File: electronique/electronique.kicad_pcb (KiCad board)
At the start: 2 copper layers, 5 parts, among them J1 Conn_02x07_Odd_Even, U1 STM32L451RETx, U2 LD1117S50TR_SOT223, U3 LD1117S33TR_SOT223

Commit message: Schema change
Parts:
- added R1: R, Resistor_SMD:R_0805_2012Metric_Pad1.20x1.40mm_HandSolder, F.Cu at (132.1, 60.3)
- added R10: R, Resistor_SMD:R_0805_2012Metric_Pad1.20x1.40mm_HandSolder, F.Cu at (142.2, 40.6)
- added R11: R, Resistor_SMD:R_0805_2012Metric_Pad1.20x1.40mm_HandSolder, F.Cu at (142.6, 48.9)
- added R2: R, Resistor_SMD:R_0805_2012Metric_Pad1.20x1.40mm_HandSolder, F.Cu at (156.8, 38.1)
- added R3: R, Resistor_SMD:R_0805_2012Metric_Pad1.20x1.40mm_HandSolder, F.Cu at (156.6, 35.6)
- added R4: R, Resistor_SMD:R_0805_2012Metric_Pad1.20x1.40mm_HandSolder, F.Cu at (156.2, 32.4)
- added R5: R, Resistor_SMD:R_0805_2012Metric_Pad1.20x1.40mm_HandSolder, F.Cu at (156.8, 29.8)
- added R6: R, Resistor_SMD:R_0805_2012Metric_Pad1.20x1.40mm_HandSolder, F.Cu at (133.7, 48.3)
- added R7: R, Resistor_SMD:R_0805_2012Metric_Pad1.20x1.40mm_HandSolder, F.Cu at (142.9, 45.1)
- moved U3 36.4 mm to (135.9, 21.6), turned to 90 degrees
- moved D1 31.4 mm to (153.7, 24.1)
- moved U2 20.6 mm to (144.8, 26.7), turned to 180 degrees
- moved U1 12.7 mm to (132.1, 38.1), turned to 90 degrees
- moved J1 9.88 mm to (123.2, 54.1)
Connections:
- net Net-(BT1-Pad1) renamed +BATT
- net Net-(J1-Pad13) renamed /RX1
- net Net-(J1-Pad14) renamed /TX1
- net Net-(U1-Pad22) renamed /M1_PWM
- net Net-(U1-Pad34) renamed /M2N_PWM
- net Net-(U1-Pad35) renamed /M2_PWM
- net Net-(U1-Pad41) renamed /ECHO1
- net Net-(U1-Pad42) renamed /ECHO2
- net Net-(U1-Pad43) renamed /TRIG_US
- net Net-(U1-Pad44) renamed /ECHO3
- net Net-(U1-Pad46) renamed /SWDIO
- net Net-(U1-Pad49) renamed /SWCLK
- net Net-(U1-Pad50) renamed /CS
- net Net-(U1-Pad51) renamed /SCK
- net Net-(U1-Pad52) renamed /MISO
- net Net-(U1-Pad53) renamed /MOSI
- net Net-(U1-Pad54) renamed /XSHUT
- net Net-(U1-Pad58) renamed /M1N_PWM
- net Net-(U1-Pad61) renamed /SCL
- net Net-(U1-Pad62) renamed /SDA
- J1 pad 12: Net-(J1-Pad12) -> /NRST
- U1 pad 10: Net-(U1-Pad10) -> /PHOTOD3
- U1 pad 11: Net-(U1-Pad11) -> /PHOTOD4
- U1 pad 12: Net-(U1-Pad12) -> GND
- U1 pad 13: Net-(U1-Pad13) -> +3V3
- U1 pad 18: Net-(U1-Pad18) -> GND
- U1 pad 19: Net-(U1-Pad19) -> +3V3
- U1 pad 27: Net-(U1-Pad27) -> /PHOTOD
- U1 pad 28: Net-(U1-Pad28) -> /LED_A
- U1 pad 29: Net-(U1-Pad29) -> /LED_B
- U1 pad 30: Net-(U1-Pad30) -> /LED_C
- U1 pad 31: Net-(U1-Pad31) -> GND
- U1 pad 32: Net-(U1-Pad32) -> +3V3
- U1 pad 47: Net-(U1-Pad47) -> GND
- U1 pad 63: Net-(U1-Pad63) -> GND
- U1 pad 64: Net-(U1-Pad64) -> +3V3
- U1 pad 7: Net-(U1-Pad7) -> /NRST
- U1 pad 8: Net-(U1-Pad8) -> /PHOTOD1
- U1 pad 9: Net-(U1-Pad9) -> /PHOTOD2

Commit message: Schema mis a jour pour la seance de projet
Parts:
- added C1: C, Capacitor_SMD:C_0805_2012Metric_Pad1.15x1.40mm_HandSolder, F.Cu at (119.0, 53.0)
- added C2: C, Capacitor_SMD:C_0805_2012Metric_Pad1.15x1.40mm_HandSolder, F.Cu at (122.0, 53.0)
- added R8: R, Resistor_THT:R_Axial_DIN0207_L6.3mm_D2.5mm_P7.62mm_Horizontal, F.Cu at (107.4, 27.6)
- added R9: R, Resistor_THT:R_Axial_DIN0207_L6.3mm_D2.5mm_P7.62mm_Horizontal, F.Cu at (107.4, 31.6)
- moved R10 15.3 mm to (132.0, 52.0), turned to 90 degrees
- moved R7 9.75 mm to (136.0, 52.0), turned to 90 degrees
- moved J1 8.41 mm to (128.0, 61.0), turned to 90 degrees
- moved U3 6.06 mm to (130.0, 23.0)
- moved R6 6.02 mm to (129.0, 52.0), turned to 90 degrees
- moved R1 5.14 mm to (136.0, 57.0), turned to 90 degrees
- moved D1 4.12 mm to (150.0, 26.0)
- moved U2 4.08 mm to (143.0, 23.0), turned to 90 degrees
- moved R11 4.05 mm to (140.0, 52.0), turned to 90 degrees

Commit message: Schema/Routage presque finis
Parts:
- added BT1: 7.2V, Connector_PinHeader_2.54mm:PinHeader_2x01_P2.54mm_Vertical, F.Cu at (25.4, 14.0)
- added C11: .1uF, Capacitor_SMD:C_0805_2012Metric_Pad1.18x1.45mm_HandSolder, F.Cu at (71.0, 35.0)
- added C12: .1uF, Capacitor_SMD:C_0805_2012Metric_Pad1.18x1.45mm_HandSolder, F.Cu at (75.0, 67.0)
- added C13: 10uF, Capacitor_Tantalum_SMD:CP_EIA-2012-12_Kemet-R_Pad1.30x1.05mm_HandSolder, F.Cu at (56.0, 65.0)
- added C14: 1uF, Capacitor_Tantalum_SMD:CP_EIA-2012-12_Kemet-R_Pad1.30x1.05mm_HandSolder, F.Cu at (152.4, 86.7)
- added C15: .01uF, Capacitor_SMD:C_0805_2012Metric_Pad1.18x1.45mm_HandSolder, F.Cu at (154.9, 86.6)
- added C3: .1uF, Capacitor_SMD:C_0805_2012Metric_Pad1.18x1.45mm_HandSolder, F.Cu at (46.0, 65.0)
- added C4: 10uF, Capacitor_Tantalum_SMD:CP_EIA-2012-12_Kemet-R_Pad1.30x1.05mm_HandSolder, F.Cu at (45.0, 53.0)
- added C5: .1uF, Capacitor_SMD:C_0805_2012Metric_Pad1.18x1.45mm_HandSolder, F.Cu at (108.2, 52.1)
- added C6: 10uF, Capacitor_Tantalum_SMD:CP_EIA-2012-12_Kemet-R_Pad1.30x1.05mm_HandSolder, F.Cu at (45.0, 49.0)
- added C7: .1uF, Capacitor_SMD:C_0805_2012Metric_Pad1.18x1.45mm_HandSolder, F.Cu at (46.0, 61.0)
- added C8: 10uF, Capacitor_Tantalum_SMD:CP_EIA-2012-12_Kemet-R_Pad1.30x1.05mm_HandSolder, F.Cu at (45.0, 45.0)
- added FB1: Ferrite_Bead_Small, Ferrite_THT:LairdTech_28C0236-0JW-10, F.Cu at (147.3, 87.6)
- added J10: PHOTOD3, Connector_JST:JST_PH_B2B-PH-K_1x02_P2.00mm_Vertical, F.Cu at (45.7, 90.2)
- added J11: PHOTOD4, Connector_JST:JST_PH_B2B-PH-K_1x02_P2.00mm_Vertical, F.Cu at (58.4, 90.2)
- added J12: Ultrason 3, Connector_PinHeader_2.54mm:PinHeader_1x04_P2.54mm_Vertical, F.Cu at (142.2, 39.4)
- added J13: Moteur 2, Connector_JST:JST_PH_B6B-PH-K_1x06_P2.00mm_Vertical, F.Cu at (97.8, 33.0)
- added J14: Moteur 1, Connector_JST:JST_PH_B6B-PH-K_1x06_P2.00mm_Vertical, F.Cu at (62.2, 26.7)
- added J3: Camera, Connector_PinHeader_2.54mm:PinHeader_1x06_P2.54mm_Vertical, F.Cu at (130.8, 33.0)
- added J4: TOF1, Connector_PinHeader_2.54mm:PinHeader_2x05_P2.54mm_Vertical, F.Cu at (116.8, 22.9)
- added J5: Conn_01x06, Connector_PinHeader_2.54mm:PinHeader_1x06_P2.54mm_Vertical, F.Cu at (81.3, 86.4)
- added J6: Ultrason 1, Connector_PinHeader_2.54mm:PinHeader_1x04_P2.54mm_Vertical, F.Cu at (137.2, 39.4)
- added J7: PHOTOD1, Connector_JST:JST_PH_B2B-PH-K_1x02_P2.00mm_Vertical, F.Cu at (64.8, 90.2)
- added J8: PHOTOD2, Connector_JST:JST_PH_B2B-PH-K_1x02_P2.00mm_Vertical, F.Cu at (52.1, 90.2)
- added J9: Ultrason 2, Connector_PinHeader_2.54mm:PinHeader_1x04_P2.54mm_Vertical, F.Cu at (132.1, 39.4)
- added SW1: SW_Push, Button_Switch_THT:SW_PUSH_6mm, F.Cu at (90.2, 61.0)
- added U4: LB1930MC-AH, lumos_minima:LB1930MC-AH, F.Cu at (88.9, 25.4)
- added U5: LB1930MC-AH, lumos_minima:LB1930MC-AH, F.Cu at (53.3, 25.4)
- C1: value C -> .1uF; footprint Capacitor_SMD:C_0805_2012Metric_Pad1.15x1.40mm_HandSolder -> Capacitor_SMD:C_0805_2012Metric_Pad1.18x1.45mm_HandSolder
- C2: value C -> 10uF; footprint Capacitor_SMD:C_0805_2012Metric_Pad1.15x1.40mm_HandSolder -> Capacitor_Tantalum_SMD:CP_EIA-2012-12_Kemet-R_Pad1.30x1.05mm_HandSolder
- J1: value Conn_02x07_Odd_Even -> Conn_01x02; footprint FTSH:SAMTEC_FTSH-107-01-L-DV-K-A -> Connector_JST:JST_PH_B2B-PH-K_1x02_P2.00mm_Vertical
- U1: value STM32L451RETx -> LD1117S50TR_SOT223; footprint Package_QFP:LQFP-64_10x10mm_P0.5mm -> Package_TO_SOT_SMD:SOT-223-3_TabPin2
- U2: value LD1117S50TR_SOT223 -> LD1117S33TR_SOT223
- U3: value LD1117S33TR_SOT223 -> STM32L451RETx; footprint Package_TO_SOT_SMD:SOT-223-3_TabPin2 -> Package_QFP:LQFP-64_10x10mm_P0.5mm
- moved R4 119.5 mm to (41.0, 64.0)
- moved R3 118.4 mm to (40.0, 56.0)
- moved R2 117.9 mm to (41.0, 60.0), turned to 0 degrees
- moved U2 117.8 mm to (25.4, 30.5), turned to 0 degrees
- moved J1 111.8 mm to (22.9, 22.9), turned to 0 degrees
- moved D1 110.7 mm to (39.4, 22.9), turned to 180 degrees
- moved R10 98.0 mm to (44.7, 96.5), turned to 0 degrees
- moved R7 95.9 mm to (51.1, 96.5), turned to 0 degrees
- moved U1 95.6 mm to (36.8, 30.5), turned to 180 degrees
- moved R11 93.8 mm to (57.4, 96.5), turned to 0 degrees
- moved R6 79.0 mm to (63.8, 96.5), turned to 0 degrees
- moved C2 76.1 mm to (46.0, 57.0), turned to 0 degrees
- moved R1 74.7 mm to (66.0, 31.0), turned to 0 degrees
- moved U3 70.9 mm to (166.4, 83.8), turned to 0 degrees
- moved C1 69.1 mm to (51.0, 65.0), turned to 0 degrees
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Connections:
- C1 pad 1: GND -> +3V3
- C1 pad 2: Net-(C1-Pad2) -> GND
- C2 pad 1: Net-(C2-Pad1) -> +3V3
- R1 pad 1: Net-(J1-Pad11) -> Net-(J2-Pad11)
- U1 pad 1: Net-(U1-Pad1) -> GND
- U1 pad 2: Net-(U1-Pad2) -> +5V
- U1 pad 3: Net-(U1-Pad3) -> Net-(D1-Pad1)
- U2 pad 2: +5V -> +3V3
- U2 pad 3: Net-(D1-Pad1) -> +5V
- U3 pad 1: GND -> +3V3
- U3 pad 2: +3V3 -> Net-(U3-Pad2)
- U3 pad 3: +5V -> Net-(U3-Pad3)
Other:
- board outline added: 100 x 50 mm

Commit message: Schema/Routage presque finis
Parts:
- moved R10 110.6 mm to (153.7, 77.2), turned to 90 degrees
- moved R7 105.8 mm to (153.7, 70.8), turned to 90 degrees
- moved J10 102.6 mm to (147.3, 76.2), turned to 0 degrees
- moved R11 101.4 mm to (153.7, 64.5), turned to 90 degrees
- moved R6 97.7 mm to (153.7, 58.1), turned to 90 degrees
- moved J8 97.4 mm to (147.3, 69.8), turned to 0 degrees
- moved J11 92.8 mm to (147.3, 63.5), turned to 0 degrees
- moved J7 88.9 mm to (147.3, 57.1), turned to 0 degrees
- moved J12 85.5 mm to (223.5, 66.0)
- moved J6 85.5 mm to (218.4, 66.0)
- moved J9 85.5 mm to (213.4, 66.0)
- moved SW1 70.1 mm to (160.0, 67.3)
- moved J3 66.0 mm to (195.6, 45.7)
- moved U3 32.9 mm to (195.6, 68.6)

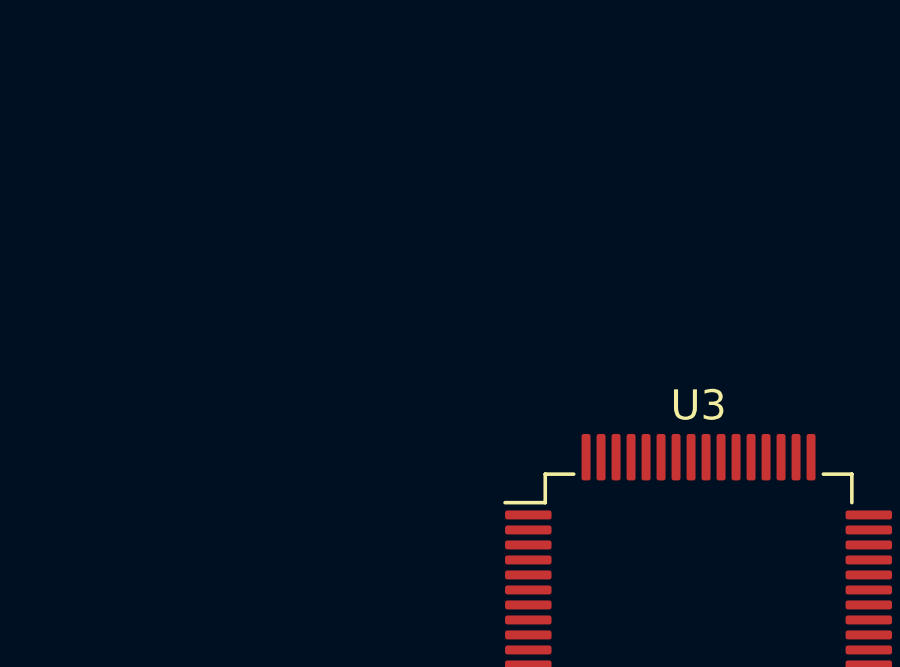
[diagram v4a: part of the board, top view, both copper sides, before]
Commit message: Ajout de l'ampli de captage de courant MAX40056.
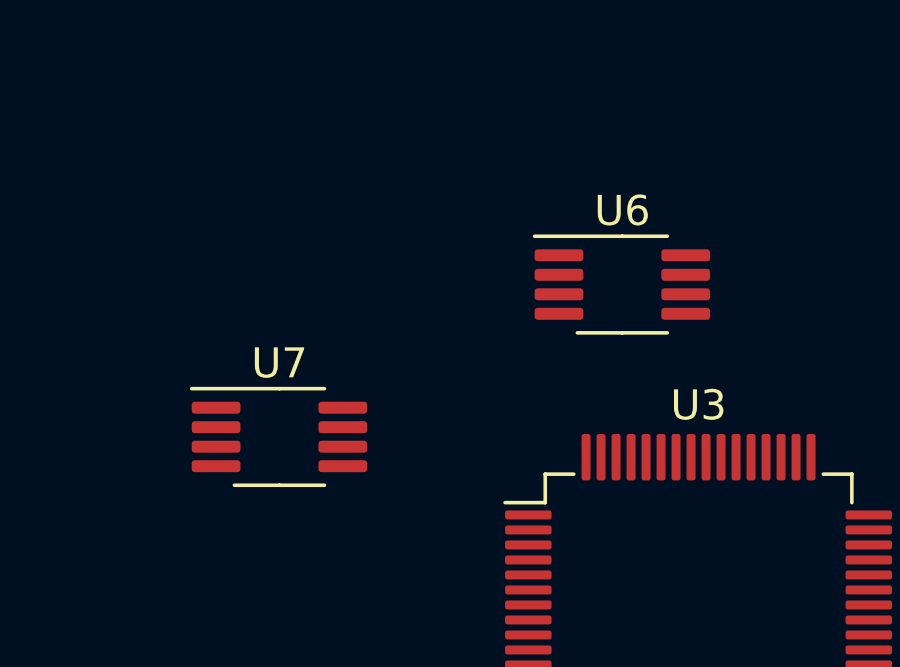
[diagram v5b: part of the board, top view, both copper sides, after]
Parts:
- added U6: MAX40056FAUA+, Package_SO:MSOP-8_3x3mm_P0.65mm, F.Cu at (193.0, 57.1)
- added U7: MAX40056FAUA+, Package_SO:MSOP-8_3x3mm_P0.65mm, F.Cu at (181.6, 62.2)
- R8, R9: value R -> 30m

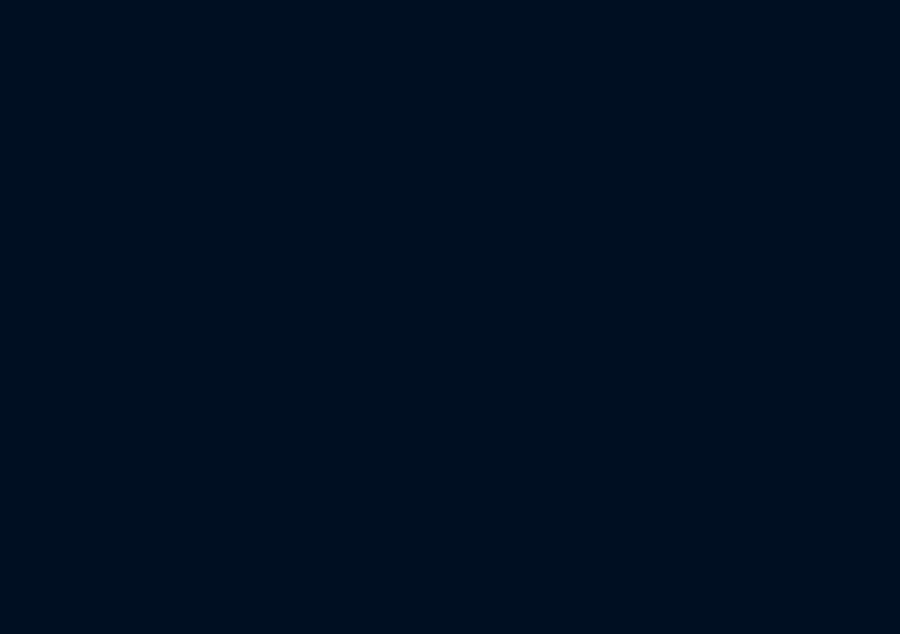
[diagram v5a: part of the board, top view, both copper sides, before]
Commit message: Cablage preliminaire des capteurs de courant
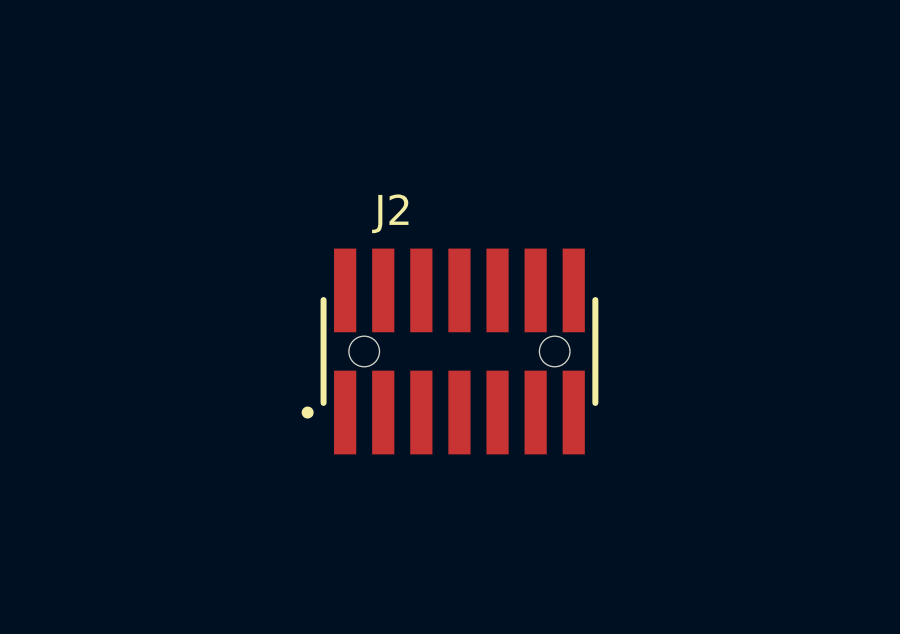
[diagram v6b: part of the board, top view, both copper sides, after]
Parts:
- added J2: Conn_02x07_Odd_Even, lumos_minima:SAMTEC_FTSH-107-01-L-DV-K-A, F.Cu at (137.2, 26.7)
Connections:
- net Net-(U6-Pad4) renamed /I_SENS1
- net Net-(U7-Pad4) renamed /I_SENS2
- J13 pad 1: Net-(J13-Pad1) -> /RSN2
- J14 pad 1: Net-(J14-Pad1) -> /RSN1
- R8 pad 1: Net-(J13-Pad1) -> /RSN2
- R8 pad 2: Net-(R8-Pad2) -> /RSP2
- R9 pad 1: Net-(J14-Pad1) -> /RSN1
- R9 pad 2: Net-(R9-Pad2) -> /RSP1
- U4 pad 9: Net-(R8-Pad2) -> /RSP2
- U5 pad 9: Net-(R9-Pad2) -> /RSP1
- U6 pad 1: Net-(U6-Pad1) -> /RSP1
- U6 pad 3: Net-(U6-Pad3) -> +3V3
- U6 pad 6: Net-(U6-Pad6) -> GND
- U6 pad 8: Net-(U6-Pad8) -> /RSN1
- U7 pad 1: Net-(U7-Pad1) -> /RSP2
- U7 pad 3: Net-(U7-Pad3) -> +3V3
- U7 pad 6: Net-(U7-Pad6) -> GND
- U7 pad 8: Net-(U7-Pad8) -> /RSN2

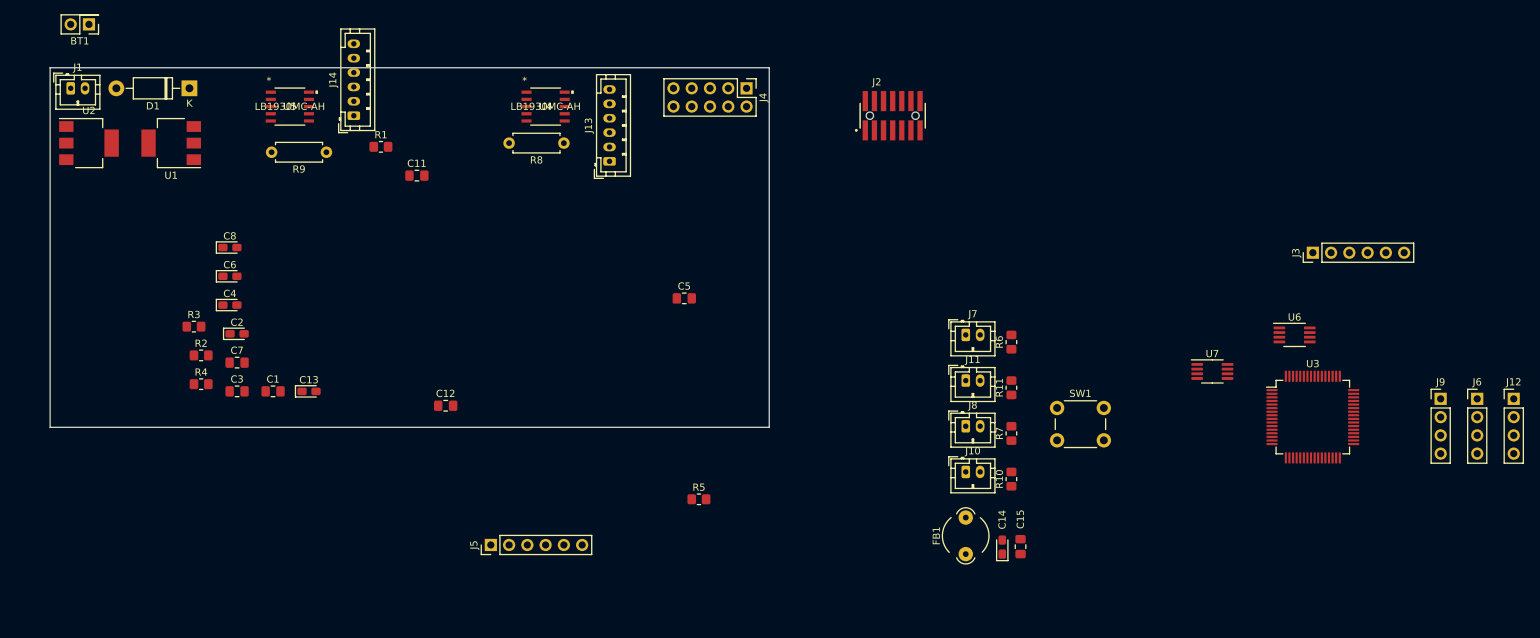
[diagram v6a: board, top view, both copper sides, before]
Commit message: Schema de concept termine, il manque les valeurs de certains condensateurs, il est possible qu'il y aie besoin de plus de condensateurs.
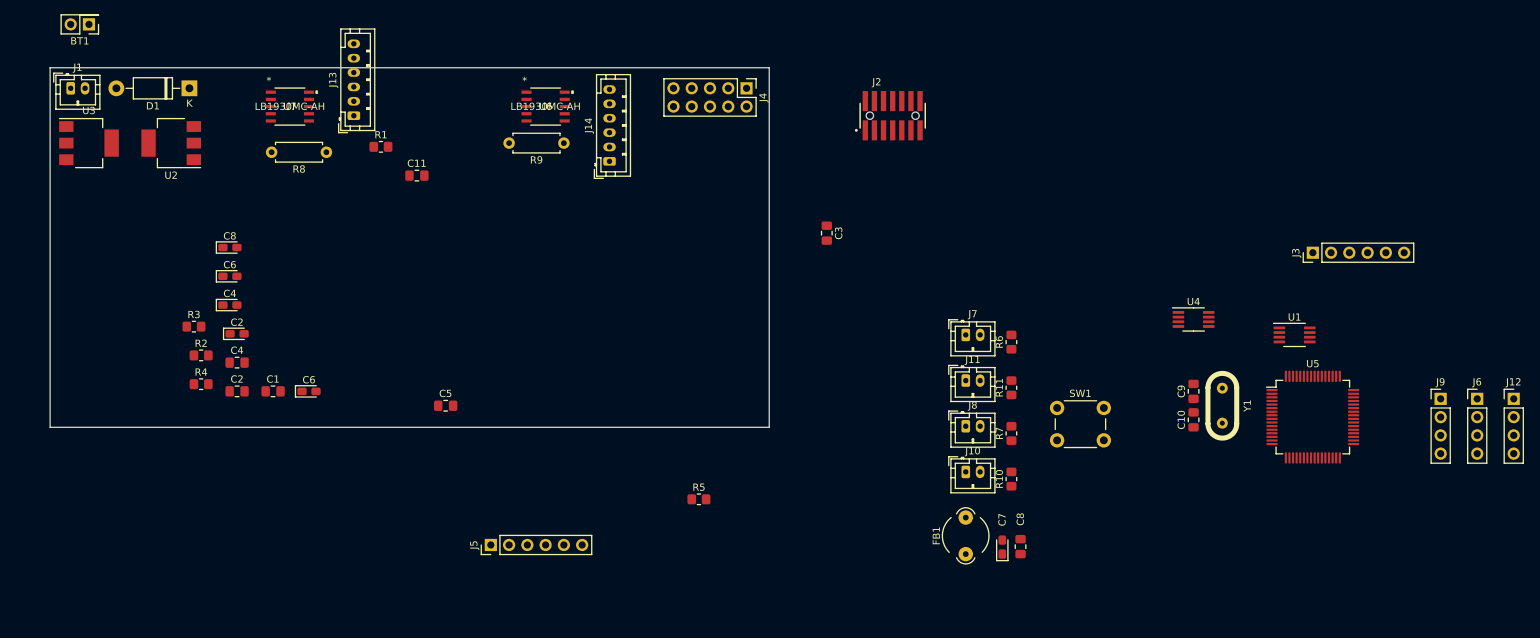
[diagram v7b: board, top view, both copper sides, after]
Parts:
- added C10: C, Capacitor_SMD:C_0805_2012Metric_Pad1.18x1.45mm_HandSolder, F.Cu at (179.0, 69.0)
- added C9: C, Capacitor_SMD:C_0805_2012Metric_Pad1.18x1.45mm_HandSolder, F.Cu at (179.0, 65.0)
- added Y1: LFXTAL003240, lumos_minima:HC494H, F.Cu at (183.0, 67.0)
- moved C3 21.8 mm to (128.0, 43.0), turned to 270 degrees
- moved U4 7.69 mm to (179.0, 55.0)
- renumbered C3 to C2, C5 to C3, C7 to C4, C12 to C5, C13 to C6, C14 to C7, C15 to C8, J14 to J13, J13 to J14, R9 to R8, R8 to R9, U6 to U1, U1 to U2, U2 to U3, U7 to U4, U3 to U5, U4 to U6, U5 to U7
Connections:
- R2 pad 2: /PHOTOD -> /PHOTOD_COUL
- U5 pad 14: Net-(U3-Pad14) -> /M2_A
- U5 pad 15: Net-(U3-Pad15) -> /M2_B
- U5 pad 23: Net-(U3-Pad23) -> /I_SENS1
- U5 pad 24: Net-(U3-Pad24) -> /I_SENS2
- U5 pad 25: Net-(U3-Pad25) -> /PHOTOD_COUL
- U5 pad 26: Net-(U3-Pad26) -> /LED_A
- U5 pad 27: /PHOTOD -> /LED_B
- U5 pad 28: /LED_A -> /LED_C
- U5 pad 29: /LED_B -> /TX1
- U5 pad 30: /LED_C -> /RX1
- U5 pad 57: Net-(U3-Pad57) -> /M1_A
- U5 pad 59: Net-(U3-Pad59) -> /M1_B

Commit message: pcb vide
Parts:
- removed the C2 at (46.0, 65.0)
- removed the C2 at (46.0, 57.0)
- removed the C4 at (46.0, 61.0)
- removed the C4 at (45.0, 53.0)
- removed the C6 at (56.0, 65.0)
- removed the C6 at (45.0, 49.0)
- removed the C8 at (154.9, 86.6)
- removed the C8 at (45.0, 45.0)
- added C2: .1uF, Capacitor_SMD:C_0805_2012Metric_Pad1.18x1.45mm_HandSolder, F.Cu at (57.4, 47.7)
- added C4: .1uF, Capacitor_SMD:C_0805_2012Metric_Pad1.18x1.45mm_HandSolder, F.Cu at (62.2, 45.9)
- added C6: 10uF, Capacitor_Tantalum_SMD:CP_EIA-2012-12_Kemet-R_Pad1.30x1.05mm_HandSolder, F.Cu at (60.1, 40.2)
- added C8: .01uF, Capacitor_SMD:C_0805_2012Metric_Pad1.18x1.45mm_HandSolder, F.Cu at (57.4, 50.7)
- R8, R9: footprint Resistor_THT:R_Axial_DIN0207_L6.3mm_D2.5mm_P7.62mm_Horizontal -> Resistor_SMD:R_1206_3216Metric_Pad1.30x1.75mm_HandSolder
- moved J12 197.2 mm to (28.3, 38.2)
- moved J9 194.2 mm to (21.1, 38.5)
- moved J6 179.8 mm to (42.7, 28.0)
- moved J3 179.5 mm to (16.4, 34.5), turned to 0 degrees
- moved U5 167.2 mm to (33.2, 28.6)
- moved U4 156.6 mm to (22.4, 50.8)
- moved Y1 138.1 mm to (50.4, 28.5), turned to 0 degrees
- moved SW1 130.3 mm to (32.6, 40.0)
- moved U1 121.0 mm to (78.8, 17.1)
- moved C9 116.4 mm to (64.9, 41.9), turned to 0 degrees
- moved C10 113.9 mm to (70.1, 35.8), turned to 0 degrees
- moved J10 108.6 mm to (42.1, 49.2)
- moved FB1 107.8 mm to (57.7, 27.8), turned to 0 degrees
- moved C7 102.1 mm to (60.1, 43.0), turned to 0 degrees
- moved J7 97.6 mm to (50.1, 48.9)
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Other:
- board outline removed
